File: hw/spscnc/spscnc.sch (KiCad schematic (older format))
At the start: 7 parts

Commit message: halfway changes to support additional axis and to extend over i2so
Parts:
- added J21: Conn_01x04, Connector_PinHeader_2.54mm:PinHeader_1x04_P2.54mm_Vertical, symbol Connector_Generic:Conn_01x04
- added J22: Conn_01x06, Connector_PinHeader_2.54mm:PinHeader_1x06_P2.54mm_Vertical, symbol Connector_Generic:Conn_01x06
- added R192: 47, Resistor_SMD:R_0805_2012Metric, symbol Device:R
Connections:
- net DIR_X: now also J22.2 (Pin_2)
- net ENABLE_STEPPERS: now also J22.4 (Pin_4)
- net SDCARD_MISO: now also R192.2
- net STEP_X: now also J22.1 (Pin_1)
- net Stepper X/STEPPER_MISO renamed A_MISO
- net A_MISO: now also J21.3 (Pin_3)
- net Stepper X/STEPPER_SCK renamed STEPPER_SCK_B
- net STEPPER_SCK_B: now also J21.2 (Pin_2)
- net Stepper X/~STEPPER_CS renamed STEPPER_CS_B
- net STEPPER_CS_B: now also J21.1 (Pin_1)
- new net +3V3: J22.3 (Pin_3)
- new net A_MOSI: J21.4 (Pin_4)
- new net Axis A/STEPPER_MISO: R192.1
- new net GND: J22.5 (Pin_5), J22.6 (Pin_6)
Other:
- note added: "PROTO REUSE OPT1\n"
- moved on the sheet: R164, R167, R36

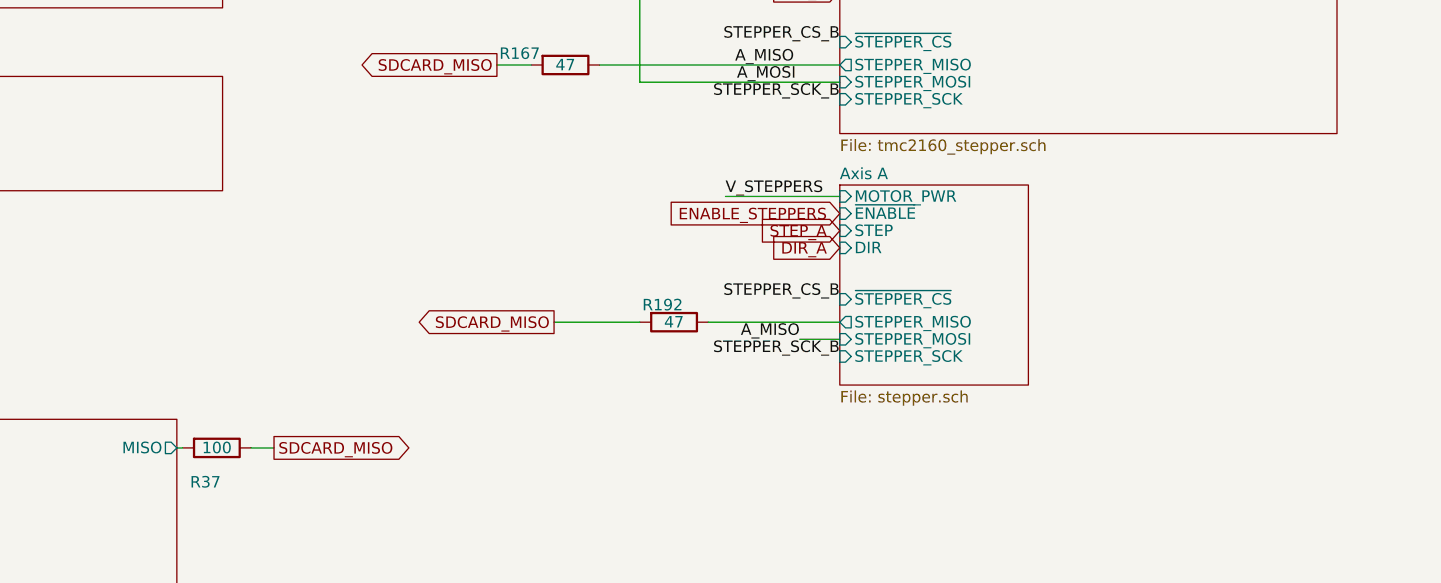
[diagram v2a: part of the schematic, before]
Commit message: added most corrections on the schematic for i2s operation.
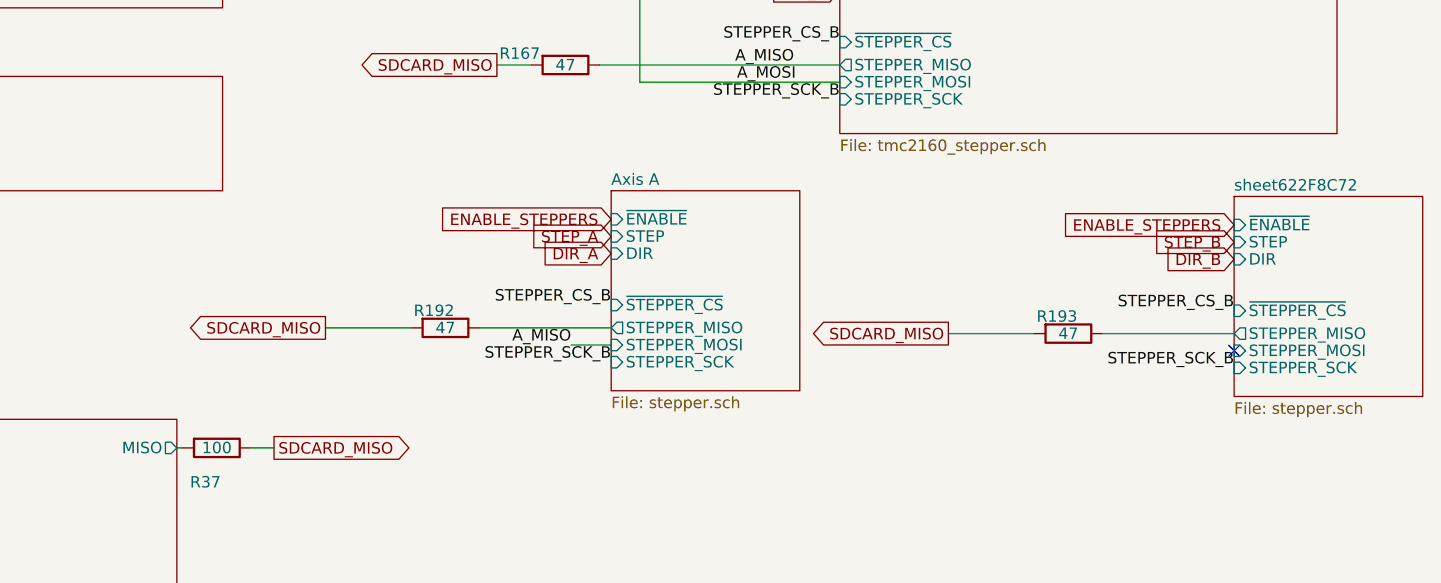
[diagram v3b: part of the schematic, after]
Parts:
- added R193: 47, Resistor_SMD:R_0805_2012Metric, symbol Device:R
- J21: jlcpcb DNP -> DNP008
- J22: jlcpcb DNP -> DNP562
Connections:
- net SDCARD_MISO: now also R193.2
- new net sheet622F8C72/STEPPER_MISO: R193.1
- no-connect marks 4 -> 5
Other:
- moved on the sheet: R192
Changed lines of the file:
@@
 $Descr A4 11693 8268
 encoding utf-8
-Sheet 1 16
+Sheet 1 17
 Title "Trinamic FluidNC CNC Controller"
 Date "2022-01-27"
@@
 Wire Wire Line
 	8075 1425 8025 1425
-Text GLabel 8400 5625 0    50   Input ~ 0
-ENABLE_STEPPERS
-Text GLabel 8400 5700 0    50   Input ~ 0
+Text GLabel 7400 5650 0    50   Input ~ 0
+ENABLE_STEPPERS
+Text GLabel 7400 5725 0    50   Input ~ 0
 STEP_A
-Text GLabel 8400 5775 0    50   Input ~ 0
+Text GLabel 7400 5800 0    50   Input ~ 0
 DIR_A
-Text Label 7900 5550 0    50   ~ 0
-V_STEPPERS
-Wire Wire Line
-	7900 5550 8400 5550
-$Sheet
-S 8400 5500 825  875
+$Sheet
+S 7400 5525 825  875
 U 6221509B
 F0 "Axis A" 50
 F1 "stepper.sch" 50
-F2 "~STEPPER_CS" I L 8400 6000 50
-F3 "STEPPER_MISO" O L 8400 6100 50
-F4 "STEPPER_MOSI" I L 8400 6175 50
-F5 "STEPPER_SCK" I L 8400 6250 50
-F6 "MOTOR_PWR" I L 8400 5550 50
-F7 "~ENABLE" I L 8400 5625 50
-F8 "STEP" I L 8400 5700 50
-F9 "DIR" I L 8400 5775 50
+F2 "~STEPPER_CS" I L 7400 6025 50
+F3 "STEPPER_MISO" O L 7400 6125 50
+F4 "STEPPER_MOSI" I L 7400 6200 50
+F5 "STEPPER_SCK" I L 7400 6275 50
+F6 "~ENABLE" I L 7400 5650 50
+F7 "STEP" I L 7400 5725 50
+F8 "DIR" I L 7400 5800 50
 $EndSheet
 $Comp
@@
 F 2 "Connector_PinHeader_2.54mm:PinHeader_1x04_P2.54mm_Vertical" H 1875 3575 50  0001 C CNN
 F 3 "~" H 1875 3575 50  0001 C CNN
-F 4 "DNP" H 1875 3575 50  0001 C CNN "jlcpcb"
+F 4 "DNP008" H 1875 3575 50  0001 C CNN "jlcpcb"
 	1    1875 3575
 	1    0    0    -1
@@
 F 2 "Connector_PinHeader_2.54mm:PinHeader_1x06_P2.54mm_Vertical" H 1875 4225 50  0001 C CNN
 F 3 "~" H 1875 4225 50  0001 C CNN
-F 4 "DNP" H 1875 4225 50  0001 C CNN "jlcpcb"
+F 4 "DNP562" H 1875 4225 50  0001 C CNN "jlcpcb"
 	1    1875 4225
 	1    0    0    -1
@@
 Wire Wire Line
 	1600 4525 1600 4425
-Text GLabel 7150 6100 0    50   Output ~ 0
+Text GLabel 6150 6125 0    50   Output ~ 0
 SDCARD_MISO
 $Comp
 L Device:R R192
 U 1 1 622AE21B
-P 7675 6100
-F 0 "R192" V 7600 6050 50  0000 C CNN
-F 1 "47" V 7675 6100 50  0000 C CNN
-F 2 "Resistor_SMD:R_0805_2012Metric" V 7605 6100 50  0001 C CNN
-F 3 "~" H 7675 6100 50  0001 C CNN
-F 4 "C17714" H 7675 6100 50  0001 C CNN "jlcpcb"
-	1    7675 6100
-	0    1    1    0
-$EndComp
-Wire Wire Line
-	7525 6100 7150 6100
-Text Label 8225 6175 2    50   ~ 0
+P 6675 6125
+F 0 "R192" V 6600 6075 50  0000 C CNN
+F 1 "47" V 6675 6125 50  0000 C CNN
+F 2 "Resistor_SMD:R_0805_2012Metric" V 6605 6125 50  0001 C CNN
+F 3 "~" H 6675 6125 50  0001 C CNN
+F 4 "C17714" H 6675 6125 50  0001 C CNN "jlcpcb"
+	1    6675 6125
+	0    1    1    0
+$EndComp
+Wire Wire Line
+	6525 6125 6150 6125
+Text Label 7225 6200 2    50   ~ 0
 A_MISO
 Wire Wire Line
-	8225 6175 8400 6175
-Wire Wire Line
-	7825 6100 8400 6100
+	7225 6200 7400 6200
+Wire Wire Line
+	6825 6125 7400 6125
 Text Notes 1275 3225 0    50   ~ 0
 PROTO REUSE OPT1\n
@@
 Text Label 8400 4875 2    50   ~ 0
 STEPPER_CS_B
-Text Label 8400 6000 2    50   ~ 0
-STEPPER_CS_B
-Text Label 8400 6250 2    50   ~ 0
+Text Label 7400 6025 2    50   ~ 0
+STEPPER_CS_B
+Text Label 7400 6275 2    50   ~ 0
 STEPPER_SCK_B
 Text Label 8400 5125 2    50   ~ 0
@@
 Text GLabel 1675 4325 0    50   Input ~ 0
 ENABLE_STEPPERS
+Text GLabel 10125 5675 0    50   Input ~ 0
+ENABLE_STEPPERS
+Text GLabel 10125 5750 0    50   Input ~ 0
+STEP_B
+Text GLabel 10125 5825 0    50   Input ~ 0
+DIR_B
+$Sheet
+S 10125 5550 825  875
+U 622F8C7E
+F0 "sheet622F8C72" 50
+F1 "stepper.sch" 50
+F2 "~STEPPER_CS" I L 10125 6050 50
+F3 "STEPPER_MISO" O L 10125 6150 50
+F4 "STEPPER_MOSI" I L 10125 6225 50
+F5 "STEPPER_SCK" I L 10125 6300 50
+F6 "~ENABLE" I L 10125 5675 50
+F7 "STEP" I L 10125 5750 50
+F8 "DIR" I L 10125 5825 50
+$EndSheet
+Text GLabel 8875 6150 0    50   Output ~ 0
+SDCARD_MISO
+$Comp
+L Device:R R193
+U 1 1 622F8C86
+P 9400 6150
+F 0 "R193" V 9325 6100 50  0000 C CNN
+F 1 "47" V 9400 6150 50  0000 C CNN
+F 2 "Resistor_SMD:R_0805_2012Metric" V 9330 6150 50  0001 C CNN
+F 3 "~" H 9400 6150 50  0001 C CNN
+F 4 "C17714" H 9400 6150 50  0001 C CNN "jlcpcb"
+	1    9400 6150
+	0    1    1    0
+$EndComp
+Wire Wire Line
+	9250 6150 8875 6150
+Wire Wire Line
+	9550 6150 10125 6150
+Text Label 10125 6050 2    50   ~ 0
+STEPPER_CS_B
+Text Label 10125 6300 2    50   ~ 0
+STEPPER_SCK_B
+NoConn ~ 10125 6225
 $EndSCHEMATC

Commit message: began routing of the i2so part
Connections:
- net A_MISO: now also J21.4 (Pin_4); no longer J21.3 (Pin_3)
- net A_MOSI: now also J21.3 (Pin_3); no longer J21.4 (Pin_4)
- net STEPPER_CS_B: now also J21.2 (Pin_2); no longer J21.1 (Pin_1)
- net STEPPER_SCK_B: now also J21.1 (Pin_1); no longer J21.2 (Pin_2)
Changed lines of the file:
@@
 Text Label 8425 1250 2    50   ~ 0
 STEPPER_CS_B
-Text Label 1575 3475 2    50   ~ 0
+Text Label 1675 3575 2    50   ~ 0
 STEPPER_CS_B
 Wire Wire Line
@@
 Wire Wire Line
 	6650 1500 8425 1500
-Text Label 1675 3575 2    50   ~ 0
+Text Label 1575 3475 2    50   ~ 0
 STEPPER_SCK_B
 Wire Wire Line
@@
 Text Label 7950 5050 0    50   ~ 0
 A_MOSI
-Text Label 1675 3775 2    50   ~ 0
+Text Label 1675 3675 2    50   ~ 0
 A_MOSI
 Wire Wire Line
@@
 Text Label 8200 4975 2    50   ~ 0
 A_MISO
-Text Label 1675 3675 2    50   ~ 0
+Text Label 1675 3775 2    50   ~ 0
 A_MISO
 Text GLabel 1675 4025 0    50   Input ~ 0

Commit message: Finished preliminary routing, pending checklist and review
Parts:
- removed R192: 47, Resistor_SMD:R_0805_2012Metric, symbol Device:R
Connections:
- no-connect marks 5 -> 4
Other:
- note added: "CHECKS:\n[OK] change fluidnc config and attempt to boot.\n[OK] check bootmode is ok with GPIO signals\ncheck pulses during boot on output pins.\nComplete electrical checklist\nThorought layout checks on copper zones and signal crosstalk\n"
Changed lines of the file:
@@
 Wire Wire Line
 	1600 4525 1600 4425
-Text GLabel 6150 6125 0    50   Output ~ 0
-SDCARD_MISO
-$Comp
-L Device:R R192
-U 1 1 622AE21B
-P 6675 6125
-F 0 "R192" V 6600 6075 50  0000 C CNN
-F 1 "47" V 6675 6125 50  0000 C CNN
-F 2 "Resistor_SMD:R_0805_2012Metric" V 6605 6125 50  0001 C CNN
-F 3 "~" H 6675 6125 50  0001 C CNN
-F 4 "C17714" H 6675 6125 50  0001 C CNN "jlcpcb"
-	1    6675 6125
-	0    1    1    0
-$EndComp
-Wire Wire Line
-	6525 6125 6150 6125
 Text Label 7225 6200 2    50   ~ 0
 A_MISO
 Wire Wire Line
 	7225 6200 7400 6200
-Wire Wire Line
-	6825 6125 7400 6125
 Text Notes 1275 3225 0    50   ~ 0
 PROTO REUSE OPT1\n
@@
 Text Label 10125 6300 2    50   ~ 0
 STEPPER_SCK_B
-NoConn ~ 10125 6225
+Wire Wire Line
+	6675 6125 6675 6500
+Wire Wire Line
+	6675 6500 9525 6500
+Wire Wire Line
+	9525 6500 9525 6225
+Wire Wire Line
+	9525 6225 10125 6225
+Wire Wire Line
+	6675 6125 7400 6125
+Text Notes 3900 8950 0    50   ~ 0
+CHECKS:\n[OK] change fluidnc config and attempt to boot.\n[OK] check bootmode is ok with GPIO signals\ncheck pulses during boot on output pins.\nComplete electrical checklist\nThorought layout checks on copper zones and signal crosstalk\n
 $EndSCHEMATC

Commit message: As ordered 1.0.1
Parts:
- JP3: jlcpcb DNP_NA0 -> DNP443
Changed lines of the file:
@@
 Sheet 1 17
 Title "Trinamic FluidNC CNC Controller"
-Date "2022-01-27"
-Rev "1.0.0"
+Date "2022-02-12"
+Rev "1.0.1"
 Comp ""
 Comment1 ""
@@
 F 2 "Connector_PinHeader_2.54mm:PinHeader_1x02_P2.54mm_Vertical" H 6900 950 50  0001 C CNN
 F 3 "~" H 6900 950 50  0001 C CNN
-F 4 "DNP_NA0" H 6900 950 50  0001 C CNN "jlcpcb"
+F 4 "DNP443" H 6900 950 50  0001 C CNN "jlcpcb"
 	1    6900 950
 	1    0    0    -1

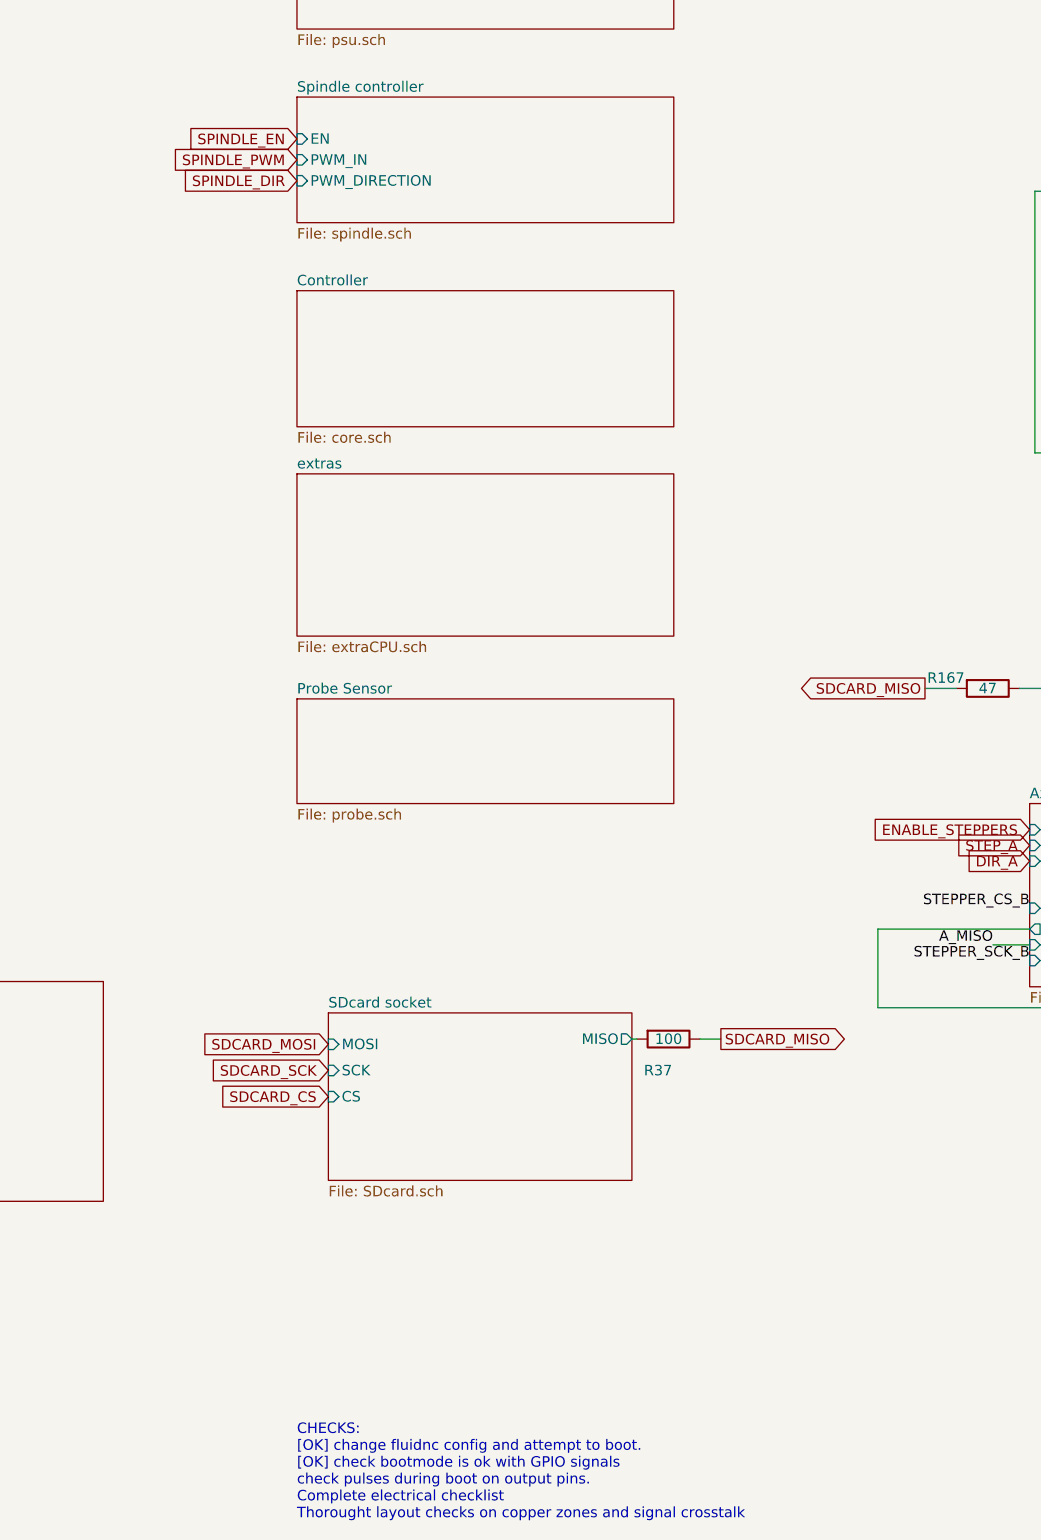
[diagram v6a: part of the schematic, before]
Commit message: Revision 1.1.0 With only critical corrections. Pending some work on the relays as that part could be remade from scratch for flexibility.
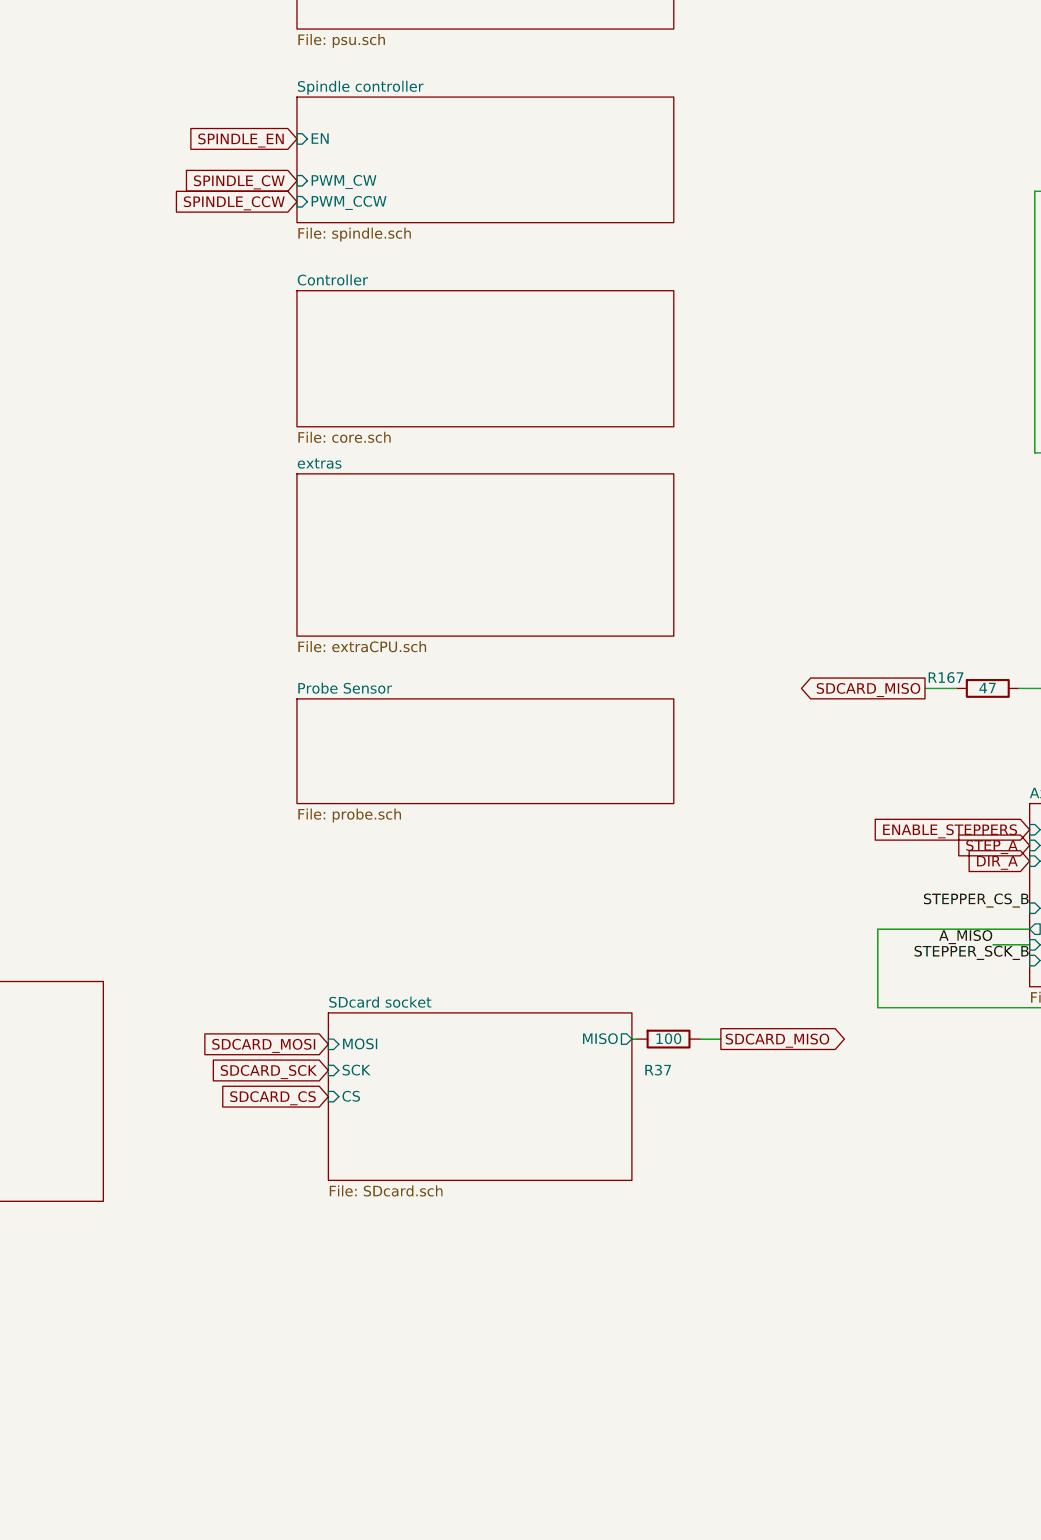
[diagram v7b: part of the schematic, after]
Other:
- note removed: "CHECKS:\n[OK] change fluidnc config and attempt to boot.\n[OK] check bootmode is ok with GPIO signals\ncheck pulses during boot on output pins.\nComplete electrical checklist\nThorought layout checks on copper zones and signal crosstalk\n"
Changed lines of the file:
@@
 Sheet 1 17
 Title "Trinamic FluidNC CNC Controller"
-Date "2022-02-12"
-Rev "1.0.1"
+Date "2022-04-29"
+Rev "1.1.0"
 Comp ""
 Comment1 ""
@@
 F1 "spindle.sch" 50
 F2 "EN" I L 3900 2350 50
-F3 "PWM_IN" I L 3900 2450 50
-F4 "PWM_DIRECTION" I L 3900 2550 50
+F3 "PWM_CW" I L 3900 2550 50
+F4 "PWM_CCW" I L 3900 2650 50
 $EndSheet
 $Sheet
@@
 Text GLabel 3900 2350 0    50   Input ~ 0
 SPINDLE_EN
-Text GLabel 3900 2450 0    50   Input ~ 0
-SPINDLE_PWM
 Text GLabel 3900 2550 0    50   Input ~ 0
-SPINDLE_DIR
+SPINDLE_CW
+Text GLabel 3900 2650 0    50   Input ~ 0
+SPINDLE_CCW
 $Sheet
 S 3900 5025 1800 500
@@
 Wire Wire Line
 	6675 6125 7400 6125
-Text Notes 3900 8950 0    50   ~ 0
-CHECKS:\n[OK] change fluidnc config and attempt to boot.\n[OK] check bootmode is ok with GPIO signals\ncheck pulses during boot on output pins.\nComplete electrical checklist\nThorought layout checks on copper zones and signal crosstalk\n
 $EndSCHEMATC
